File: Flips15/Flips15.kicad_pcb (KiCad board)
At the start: 2 copper layers, 100 x 100 mm, 62 parts, among them U1001 74HC238, U1002 ULN2803A, U1003 74HC238, U1004 TBD62783A, U1101 74HC238, U1102 ULN2803A, U1103 74HC238, U1104 TBD62783A, U201 74LS138, U301 74HC238, U302 ULN2803A, U303 74HC238, U304 TBD62783A, U401 74HC238, U402 ULN2803A, U403 74HC238, U404 TBD62783A, U501 74HC238, U502 ULN2803A, U503 74HC238, U504 TBD62783A, U601 74HC238, U602 ULN2803A, U603 74HC238, U604 TBD62783A, U701 74LS138, U801 74HC238, U802 ULN2803A, U803 74HC238, U804 TBD62783A, U901 74HC238, U902 ULN2803A, U903 74HC238, U904 TBD62783A

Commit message: rework Flips15 draft
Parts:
- U1001, U1003, U1101, U1103, U301, U303, U401, U403, U501, U503, U601, U603, U801, U803, U901, U903: footprint SMD_Packages:SO-16-N -> Housings_SOIC:SOIC-16_3.9x9.9mm_Pitch1.27mm
- U201, U701: value 74LS138 -> 74HC238; footprint SMD_Packages:SO-16-N -> Housings_SOIC:SOIC-16_3.9x9.9mm_Pitch1.27mm
- moved C701 331.5 mm to (88.9, 141.6), turned to 90 degrees
- moved C902 283.5 mm to (64.8, 131.4), turned to 180 degrees
- moved C901 281.3 mm to (101.0, 131.4), turned to 180 degrees
- moved C1101 247.8 mm to (137.8, 131.4), turned to 180 degrees
- moved C302 247.5 mm to (255.4, 120.0)
- moved C301 247.5 mm to (266.7, 105.0)
- moved C1102 234.9 mm to (127.0, 131.4), turned to 180 degrees
- moved C802 232.8 mm to (53.3, 131.4), turned to 180 degrees
- moved C1002 226.9 mm to (76.2, 131.4), turned to 180 degrees
- moved C1001 225.5 mm to (113.0, 131.4), turned to 180 degrees
- moved C801 210.4 mm to (89.5, 131.4), turned to 180 degrees
- moved U201 66.2 mm to (195.6, 132.1), turned to 90 degrees
- moved CNX101 63.5 mm to (198.1, 146.1)
- moved BROSE103 47.3 mm to (117.5, 99.1)
- moved U1004 29.3 mm to (85.1, 108.6)
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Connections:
- net Net-(U1001-Pad10) renamed /UnitY/Group2/YL5
- net Net-(U1001-Pad11) renamed /UnitY/Group2/YL4
- net Net-(U1001-Pad12) renamed /UnitY/Group2/YL3
- net Net-(U1001-Pad13) renamed /UnitY/Group2/YL2
- net Net-(U1001-Pad14) renamed /UnitY/Group2/YL1
- net Net-(U1001-Pad15) renamed /UnitY/Group2/YL0
- net Net-(U1001-Pad7) renamed /UnitY/Group2/YL7
- net Net-(U1001-Pad9) renamed /UnitY/Group2/YL6
- net Net-(U1003-Pad10) renamed /UnitY/Group2/YH5
- net Net-(U1003-Pad11) renamed /UnitY/Group2/YH4
- net Net-(U1003-Pad12) renamed /UnitY/Group2/YH3
- net Net-(U1003-Pad13) renamed /UnitY/Group2/YH2
- net Net-(U1003-Pad14) renamed /UnitY/Group2/YH1
- net Net-(U1003-Pad15) renamed /UnitY/Group2/YH0
- net Net-(U1003-Pad7) renamed /UnitY/Group2/YH7
- net Net-(U1003-Pad9) renamed /UnitY/Group2/YH6
- net Net-(U1101-Pad10) renamed /UnitY/Group3/YL5
- net Net-(U1101-Pad11) renamed /UnitY/Group3/YL4
- net Net-(U1101-Pad12) renamed /UnitY/Group3/YL3
- net Net-(U1101-Pad13) renamed /UnitY/Group3/YL2
- net Net-(U1101-Pad14) renamed /UnitY/Group3/YL1
- net Net-(U1101-Pad15) renamed /UnitY/Group3/YL0
- net Net-(U1101-Pad7) renamed /UnitY/Group3/YL7
- net Net-(U1101-Pad9) renamed /UnitY/Group3/YL6
- net Net-(U1103-Pad10) renamed /UnitY/Group3/YH5
- net Net-(U1103-Pad11) renamed /UnitY/Group3/YH4
- net Net-(U1103-Pad12) renamed /UnitY/Group3/YH3
- net Net-(U1103-Pad13) renamed /UnitY/Group3/YH2
- net Net-(U1103-Pad14) renamed /UnitY/Group3/YH1
- net Net-(U1103-Pad15) renamed /UnitY/Group3/YH0
- net Net-(U1103-Pad7) renamed /UnitY/Group3/YH7
- net Net-(U1103-Pad9) renamed /UnitY/Group3/YH6
- net Net-(U301-Pad10) renamed /UnitX/Group0/YL5
- net Net-(U301-Pad11) renamed /UnitX/Group0/YL4
- net Net-(U301-Pad12) renamed /UnitX/Group0/YL3
- net Net-(U301-Pad13) renamed /UnitX/Group0/YL2
- net Net-(U301-Pad14) renamed /UnitX/Group0/YL1
- net Net-(U301-Pad15) renamed /UnitX/Group0/YL0
- net Net-(U301-Pad7) renamed /UnitX/Group0/YL7
- net Net-(U301-Pad9) renamed /UnitX/Group0/YL6
- net Net-(U303-Pad10) renamed /UnitX/Group0/YH5
- net Net-(U303-Pad11) renamed /UnitX/Group0/YH4
- net Net-(U303-Pad12) renamed /UnitX/Group0/YH3
- net Net-(U303-Pad13) renamed /UnitX/Group0/YH2
- net Net-(U303-Pad14) renamed /UnitX/Group0/YH1
- net Net-(U303-Pad15) renamed /UnitX/Group0/YH0
- net Net-(U303-Pad7) renamed /UnitX/Group0/YH7
- net Net-(U303-Pad9) renamed /UnitX/Group0/YH6
- net Net-(U401-Pad10) renamed /UnitX/Group1/YL5
- net Net-(U401-Pad11) renamed /UnitX/Group1/YL4
- net Net-(U401-Pad12) renamed /UnitX/Group1/YL3
- net Net-(U401-Pad13) renamed /UnitX/Group1/YL2
- net Net-(U401-Pad14) renamed /UnitX/Group1/YL1
- net Net-(U401-Pad15) renamed /UnitX/Group1/YL0
- net Net-(U401-Pad7) renamed /UnitX/Group1/YL7
- net Net-(U401-Pad9) renamed /UnitX/Group1/YL6
- net Net-(U403-Pad10) renamed /UnitX/Group1/YH5
- net Net-(U403-Pad11) renamed /UnitX/Group1/YH4
- net Net-(U403-Pad12) renamed /UnitX/Group1/YH3
- net Net-(U403-Pad13) renamed /UnitX/Group1/YH2
- net Net-(U403-Pad14) renamed /UnitX/Group1/YH1
- net Net-(U403-Pad15) renamed /UnitX/Group1/YH0
- net Net-(U403-Pad7) renamed /UnitX/Group1/YH7
- net Net-(U403-Pad9) renamed /UnitX/Group1/YH6
- net Net-(U501-Pad10) renamed /UnitX/Group2/YL5
- net Net-(U501-Pad11) renamed /UnitX/Group2/YL4
- net Net-(U501-Pad12) renamed /UnitX/Group2/YL3
- net Net-(U501-Pad13) renamed /UnitX/Group2/YL2
- net Net-(U501-Pad14) renamed /UnitX/Group2/YL1
- net Net-(U501-Pad15) renamed /UnitX/Group2/YL0
- net Net-(U501-Pad7) renamed /UnitX/Group2/YL7
- net Net-(U501-Pad9) renamed /UnitX/Group2/YL6
- net Net-(U503-Pad10) renamed /UnitX/Group2/YH5
- net Net-(U503-Pad11) renamed /UnitX/Group2/YH4
- net Net-(U503-Pad12) renamed /UnitX/Group2/YH3
- net Net-(U503-Pad13) renamed /UnitX/Group2/YH2
- net Net-(U503-Pad14) renamed /UnitX/Group2/YH1
- net Net-(U503-Pad15) renamed /UnitX/Group2/YH0
- net Net-(U503-Pad7) renamed /UnitX/Group2/YH7
- net Net-(U503-Pad9) renamed /UnitX/Group2/YH6
- net Net-(U601-Pad10) renamed /UnitX/Group3/YL5
- net Net-(U601-Pad11) renamed /UnitX/Group3/YL4
- net Net-(U601-Pad12) renamed /UnitX/Group3/YL3
- net Net-(U601-Pad13) renamed /UnitX/Group3/YL2
- net Net-(U601-Pad14) renamed /UnitX/Group3/YL1
- net Net-(U601-Pad15) renamed /UnitX/Group3/YL0
- net Net-(U601-Pad7) renamed /UnitX/Group3/YL7
- net Net-(U601-Pad9) renamed /UnitX/Group3/YL6
- net Net-(U603-Pad10) renamed /UnitX/Group3/YH5
- net Net-(U603-Pad11) renamed /UnitX/Group3/YH4
- net Net-(U603-Pad12) renamed /UnitX/Group3/YH3
- net Net-(U603-Pad13) renamed /UnitX/Group3/YH2
- net Net-(U603-Pad14) renamed /UnitX/Group3/YH1
- net Net-(U603-Pad15) renamed /UnitX/Group3/YH0
- net Net-(U603-Pad7) renamed /UnitX/Group3/YH7
- net Net-(U603-Pad9) renamed /UnitX/Group3/YH6
- net Net-(U801-Pad10) renamed /UnitY/Group0/YL5
- net Net-(U801-Pad11) renamed /UnitY/Group0/YL4
- net Net-(U801-Pad12) renamed /UnitY/Group0/YL3
- net Net-(U801-Pad13) renamed /UnitY/Group0/YL2
- net Net-(U801-Pad14) renamed /UnitY/Group0/YL1
- net Net-(U801-Pad15) renamed /UnitY/Group0/YL0
- net Net-(U801-Pad7) renamed /UnitY/Group0/YL7
- net Net-(U801-Pad9) renamed /UnitY/Group0/YL6
- net Net-(U803-Pad10) renamed /UnitY/Group0/YH5
- net Net-(U803-Pad11) renamed /UnitY/Group0/YH4
- net Net-(U803-Pad12) renamed /UnitY/Group0/YH3
- net Net-(U803-Pad13) renamed /UnitY/Group0/YH2
- net Net-(U803-Pad14) renamed /UnitY/Group0/YH1
- net Net-(U803-Pad15) renamed /UnitY/Group0/YH0
- net Net-(U803-Pad7) renamed /UnitY/Group0/YH7
- net Net-(U803-Pad9) renamed /UnitY/Group0/YH6
- net Net-(U901-Pad10) renamed /UnitY/Group1/YL5
- net Net-(U901-Pad11) renamed /UnitY/Group1/YL4
- net Net-(U901-Pad12) renamed /UnitY/Group1/YL3
- net Net-(U901-Pad13) renamed /UnitY/Group1/YL2
- net Net-(U901-Pad14) renamed /UnitY/Group1/YL1
- net Net-(U901-Pad15) renamed /UnitY/Group1/YL0
- net Net-(U901-Pad7) renamed /UnitY/Group1/YL7
- net Net-(U901-Pad9) renamed /UnitY/Group1/YL6
- net Net-(U903-Pad10) renamed /UnitY/Group1/YH5
- net Net-(U903-Pad11) renamed /UnitY/Group1/YH4
- net Net-(U903-Pad12) renamed /UnitY/Group1/YH3
- net Net-(U903-Pad13) renamed /UnitY/Group1/YH2
- net Net-(U903-Pad14) renamed /UnitY/Group1/YH1
- net Net-(U903-Pad15) renamed /UnitY/Group1/YH0
- net Net-(U903-Pad7) renamed /UnitY/Group1/YH7
- net Net-(U903-Pad9) renamed /UnitY/Group1/YH6
- U1001 pad 4: /UnitY/Group2/~GE -> GND
- U1001 pad 5: /UnitY/DATA -> GND
- U1001 pad 6: VCC -> /UnitY/E2L
- U1003 pad 4: /UnitY/Group2/~GE -> GND
- U1003 pad 6: /UnitY/DATA -> /UnitY/E2H
- U1101 pad 4: /UnitY/Group3/~GE -> GND
- U1101 pad 5: /UnitY/DATA -> GND
- U1101 pad 6: VCC -> /UnitY/E3L
- U1103 pad 4: /UnitY/Group3/~GE -> GND
- U1103 pad 6: /UnitY/DATA -> /UnitY/E3H
- U201 pad 1: /UnitX/B0 -> /UnitX/DATA
- U201 pad 10: Net-(U201-Pad10) -> /UnitX/E2H
- U201 pad 11: Net-(U201-Pad11) -> /UnitX/E2L
- U201 pad 12: /UnitX/Group3/~GE -> /UnitX/E1H
- U201 pad 13: /UnitX/Group2/~GE -> /UnitX/E1L
- U201 pad 14: /UnitX/Group1/~GE -> /UnitX/E0H
- U201 pad 15: /UnitX/Group0/~GE -> /UnitX/E0L
- U201 pad 2: /UnitX/B1 -> /UnitX/B0
- U201 pad 3: GND -> /UnitX/B1
- U201 pad 7: Net-(U201-Pad7) -> /UnitX/E3H
- U201 pad 9: Net-(U201-Pad9) -> /UnitX/E3L
- U301 pad 4: /UnitX/Group0/~GE -> GND
- U301 pad 5: /UnitX/DATA -> GND
- U301 pad 6: VCC -> /UnitX/E0L
- U303 pad 4: /UnitX/Group0/~GE -> GND
- U303 pad 6: /UnitX/DATA -> /UnitX/E0H
- U401 pad 4: /UnitX/Group1/~GE -> GND
- U401 pad 5: /UnitX/DATA -> GND
- U401 pad 6: VCC -> /UnitX/E1L
- U403 pad 4: /UnitX/Group1/~GE -> GND
- U403 pad 6: /UnitX/DATA -> /UnitX/E1H
- U501 pad 4: /UnitX/Group2/~GE -> GND
- U501 pad 5: /UnitX/DATA -> GND
- U501 pad 6: VCC -> /UnitX/E2L
- U503 pad 4: /UnitX/Group2/~GE -> GND
- U503 pad 6: /UnitX/DATA -> /UnitX/E2H
- U601 pad 4: /UnitX/Group3/~GE -> GND
- U601 pad 5: /UnitX/DATA -> GND
- U601 pad 6: VCC -> /UnitX/E3L
- U603 pad 4: /UnitX/Group3/~GE -> GND
- U603 pad 6: /UnitX/DATA -> /UnitX/E3H
- U701 pad 1: /UnitY/B0 -> /UnitY/DATA
- U701 pad 10: Net-(U701-Pad10) -> /UnitY/E2H
- U701 pad 11: Net-(U701-Pad11) -> /UnitY/E2L
- U701 pad 12: /UnitY/Group3/~GE -> /UnitY/E1H
- U701 pad 13: /UnitY/Group2/~GE -> /UnitY/E1L
- U701 pad 14: /UnitY/Group1/~GE -> /UnitY/E0H
- U701 pad 15: /UnitY/Group0/~GE -> /UnitY/E0L
- U701 pad 2: /UnitY/B1 -> /UnitY/B0
- U701 pad 3: GND -> /UnitY/B1
- U701 pad 7: Net-(U701-Pad7) -> /UnitY/E3H
- U701 pad 9: Net-(U701-Pad9) -> /UnitY/E3L
- U801 pad 4: /UnitY/Group0/~GE -> GND
- U801 pad 5: /UnitY/DATA -> GND
- U801 pad 6: VCC -> /UnitY/E0L
- U803 pad 4: /UnitY/Group0/~GE -> GND
- U803 pad 6: /UnitY/DATA -> /UnitY/E0H
- U901 pad 4: /UnitY/Group1/~GE -> GND
- U901 pad 5: /UnitY/DATA -> GND
- U901 pad 6: VCC -> /UnitY/E1L
- U903 pad 4: /UnitY/Group1/~GE -> GND
- U903 pad 6: /UnitY/DATA -> /UnitY/E1H
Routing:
- net /UnitX/Group2/YH0: track 28.6 -> 0.00 mm
- net /UnitX/Group2/YL0: track 26.7 -> 0.00 mm
- net /UnitX/Group2/YH1: track 23.3 -> 0.00 mm
- net /UnitX/Group2/YL1: track 22.8 -> 0.00 mm
- net /UnitX/Group2/YH2: track 20.3 -> 0.00 mm
- net /UnitX/Group2/YL2: track 19.7 -> 0.00 mm
- net /UnitX/Group2/YH3: track 17.2 -> 0.00 mm
- net /UnitX/Group2/YL3: track 17.1 -> 0.00 mm
- net /UnitX/Group2/YL4: track 14.7 -> 0.00 mm
- net /UnitX/Group2/YL7: track 14.7 -> 0.00 mm
- net /UnitX/Group2/YH4: track 14.7 -> 0.00 mm
- net /UnitX/Group2/YH5: track 14.0 -> 0.00 mm
- net /UnitX/Group2/YH7: track 13.3 -> 0.00 mm
- net /UnitX/Group2/YL5: track 12.4 -> 0.00 mm
- net /X21: track 12.0 -> 0.00 mm
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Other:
- net class DrivingCurrent added: clearance 0.2, trace_width 0.5, via_dia 0.8, via_drill 0.4

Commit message: Flips15 to only use 1 unit
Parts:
- removed BRDIC101, BROSE102: Conn_02x17_Odd_Even, Own:Pin_Header_Angle_Shrouded_2x17_Pitch2.54mm_ConvNumbering
- removed BROSE101: Conn_02x30_Odd_Even, Own:Pin_Header_Straight_Shrouded_2x30_Pitch2.54mm_ConvNumbering
- removed BROSE103: Conn_02x10_Odd_Even, Own:Pin_Header_Straight_Shrouded_2x10_Pitch2.54mm_ConvNumbering
- removed C201, C301, C302, C401, C402, C501, C502, C601, C602: 0μ1, Capacitors_SMD:C_0805_HandSoldering
- removed CNX101, CNY101: UFP2810, Own:Pin_Header_Angle_Shrouded_2x05_Pitch2.54mm_ConvNumbering
- removed REF** (x4): MountingHole_3.2mm_M3, Mounting_Holes:MountingHole_3.2mm_M3
- removed U201, U301, U303, U401, U403, U501, U503, U601, U603: 74HC238, Housings_SOIC:SOIC-16_3.9x9.9mm_Pitch1.27mm
- removed U302, U402, U502, U602: ULN2803A, Housings_DIP:DIP-18_W7.62mm_Socket
- removed U304, U404, U504, U604: TBD62783A, Housings_DIP:DIP-18_W7.62mm_Socket
- added BRDIC1: Conn_02x17_Odd_Even, Own:Pin_Header_Straight_Shrouded_Locks_2x17_Pitch2.54mm_ConvNumbering, F.Cu at (138.4, 64.8)
- added BROSE20: Conn_02x10_Odd_Even, Own:Pin_Header_Straight_Shrouded_Locks_2x10_Pitch2.54mm_ConvNumbering, F.Cu at (115.6, 100.3)
- added BROSE34: Conn_02x17_Odd_Even, Own:Pin_Header_Straight_Shrouded_Locks_2x17_Pitch2.54mm_ConvNumbering, F.Cu at (80.0, 57.1)
- added BROSE60: Conn_02x30_Odd_Even, Own:Pin_Header_Straight_Shrouded_Locks_2x30_Pitch2.54mm_ConvNumbering, F.Cu at (64.8, 90.2)
- added CN1: UFP2810, Own:Pin_Header_Angle_Shrouded_2x05_Pitch2.54mm_ConvNumbering, F.Cu at (102.1, 17.5)
- added JP101: Jumper_NO_Small, Own:SolderJumper1.3mm, B.Cu at (131.1, 10.7)
- added JP102: Jumper_NO_Small, Own:SolderJumper1.3mm, F.Cu at (131.4, 23.5)
- added JP103: Jumper_NO_Small, Own:SolderJumper1.3mm, F.Cu at (137.3, 10.5)
- added JP104: Jumper_NO_Small, Own:SolderJumper1.3mm, F.Cu at (131.4, 34.5)
- added JP105: Jumper_NO_Small, Own:SolderJumper1.3mm, F.Cu at (137.8, 23.5)
- added JP106: Jumper_NO_Small, Own:SolderJumper1.3mm, F.Cu at (144.7, 10.5)
- added JP107: Jumper_NO_Small, Own:SolderJumper1.3mm, F.Cu at (131.4, 41.9)
- added JP108: Jumper_NO_Small, Own:SolderJumper1.3mm, F.Cu at (137.8, 34.5)
- added JP109: Jumper_NO_Small, Own:SolderJumper1.3mm, F.Cu at (145.2, 23.5)
- added JP110: Jumper_NO_Small, Own:SolderJumper1.3mm, F.Cu at (149.5, 10.5)
- added JP111: Jumper_NO_Small, Own:SolderJumper1.3mm, F.Cu at (137.8, 41.9)
- added JP112: Jumper_NO_Small, Own:SolderJumper1.3mm, F.Cu at (145.2, 34.5)
- added JP113: Jumper_NO_Small, Own:SolderJumper1.3mm, F.Cu at (150.0, 23.5)
- added JP114: Jumper_NO_Small, Own:SolderJumper1.3mm, F.Cu at (155.9, 10.5)
- added JP115: Jumper_NO_Small, Own:SolderJumper1.3mm, F.Cu at (145.2, 41.9)
- added JP116: Jumper_NO_Small, Own:SolderJumper1.3mm, F.Cu at (150.0, 34.5)
- added JP117: Jumper_NO_Small, Own:SolderJumper1.3mm, F.Cu at (156.4, 23.5)
- added JP118: Jumper_NO_Small, Own:SolderJumper1.3mm, F.Cu at (164.0, 10.5)
- added JP119: Jumper_NO_Small, Own:SolderJumper1.3mm, F.Cu at (150.0, 41.9)
- added JP120: Jumper_NO_Small, Own:SolderJumper1.3mm, F.Cu at (156.4, 34.5)
- added JP121: Jumper_NO_Small, Own:SolderJumper1.3mm, F.Cu at (164.6, 23.5)
- added JP122: Jumper_NO_Small, Own:SolderJumper1.3mm, B.Cu at (115.6, 73.7)
- added JP123: Jumper_NO_Small, Own:SolderJumper1.3mm, F.Cu at (156.4, 41.9)
- added JP124: Jumper_NO_Small, Own:SolderJumper1.3mm, F.Cu at (164.6, 34.5)
- added JP125: Jumper_NO_Small, Own:SolderJumper1.3mm, F.Cu at (172.7, 23.5)
- added JP126: Jumper_NO_Small, Own:SolderJumper1.3mm, F.Cu at (164.6, 41.9)
- added JP127: Jumper_NO_Small, Own:SolderJumper1.3mm, F.Cu at (172.7, 34.5)
- added JP128: Jumper_NO_Small, Own:SolderJumper1.3mm, F.Cu at (172.7, 41.9)
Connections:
- U1002 pad 11: /~RY21 -> /X21
- U1002 pad 12: /~RY20 -> /X20
- U1002 pad 13: /~RY19 -> /X19
- U1002 pad 14: /~RY18 -> /X18
- U1002 pad 15: /~RY17 -> /X17
- U1002 pad 16: /~RY16 -> /X16
- U1002 pad 17: /~RY15 -> /X15
- U1102 pad 11: /~RY28 -> /X28
- U1102 pad 12: /~RY27 -> /X27
- U1102 pad 13: /~RY26 -> /X26
- U1102 pad 14: /~RY25 -> /X25
- U1102 pad 15: /~RY24 -> /X24
- U1102 pad 16: /~RY23 -> /X23
- U1102 pad 17: /~RY22 -> /X22
- U802 pad 11: /~RY7 -> /X7
- U802 pad 12: /~RY6 -> /X6
- U802 pad 13: /~RY5 -> /X5
- U802 pad 14: /~RY4 -> /X4
- U802 pad 15: /~RY3 -> /X3
- U802 pad 16: /~RY2 -> /X2
- U802 pad 17: /~RY1 -> /X1
- U902 pad 11: /~RY14 -> /X14
- U902 pad 12: /~RY13 -> /X13
- U902 pad 13: /~RY12 -> /X12
- U902 pad 14: /~RY11 -> /X11
- U902 pad 15: /~RY10 -> /X10
- U902 pad 16: /~RY9 -> /X9
- U902 pad 17: /~RY8 -> /X8

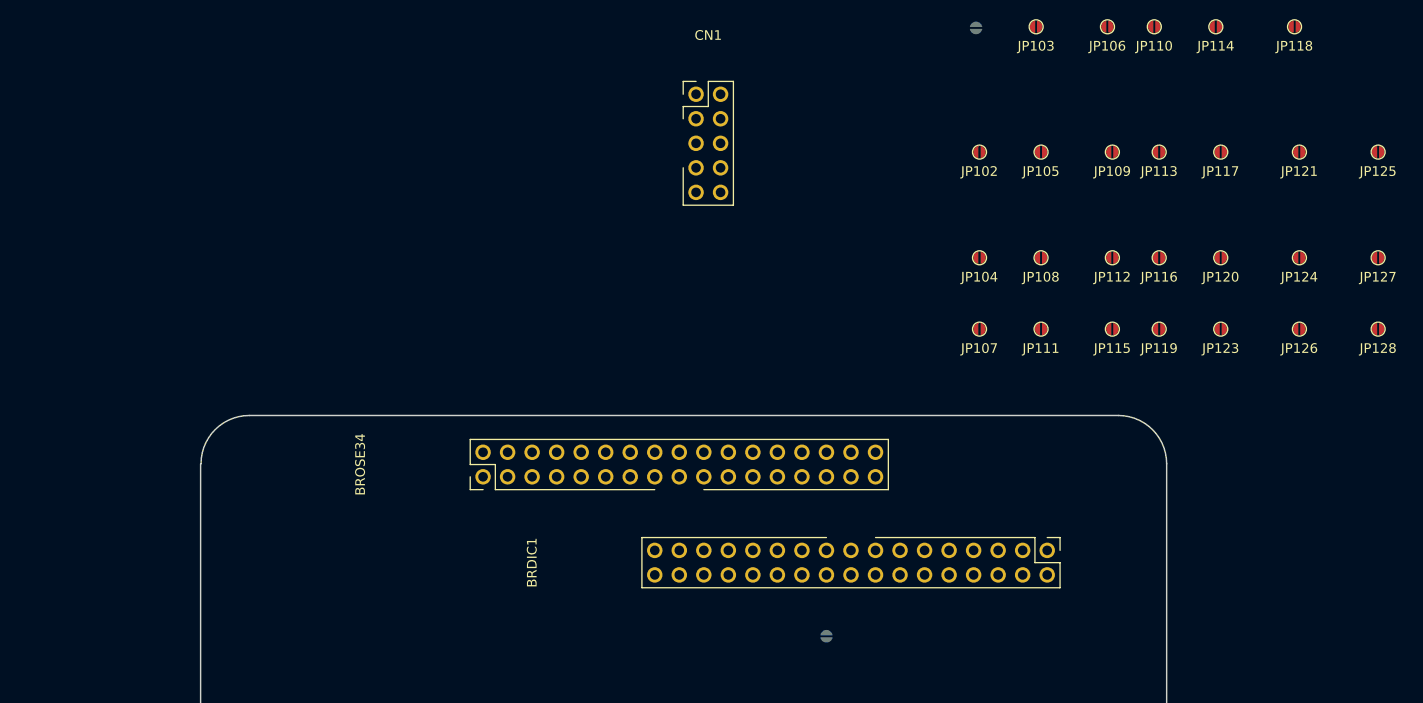
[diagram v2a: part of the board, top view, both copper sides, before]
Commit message: experimenting with solder jumpers at BRDIC1 connector
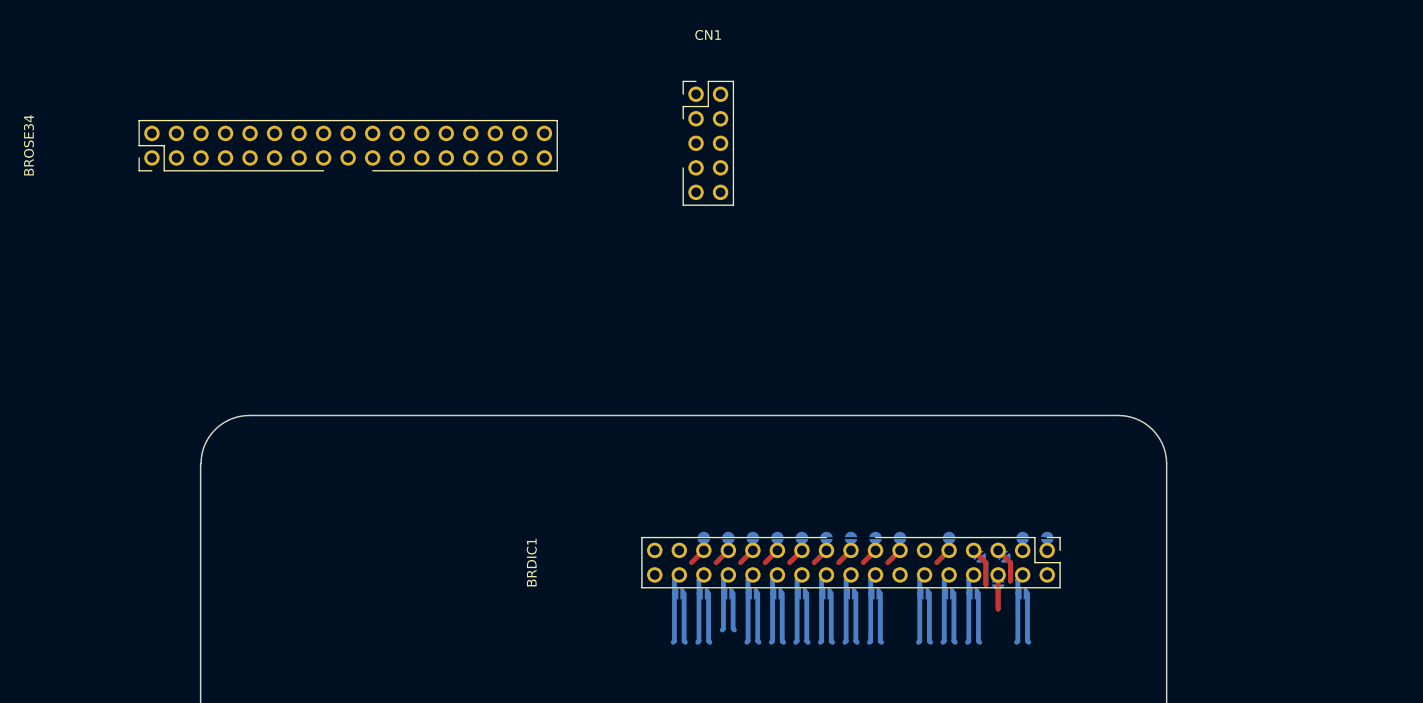
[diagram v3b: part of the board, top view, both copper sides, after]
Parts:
- JP101, JP122: footprint Own:SolderJumper1.3mm -> Own:SolderJumper1.3mmNoSilk
- JP102, JP103, JP104, JP105, JP106, JP107, JP108, JP109, JP110, JP111, JP112, JP113, JP114, JP115, JP116, JP117, JP118, JP119, JP120, JP121, JP123, JP124, JP125, JP126, JP127, JP128: footprint Own:SolderJumper1.3mm -> Own:SolderJumper1.3mmNoSilk; moved to B.Cu
- moved JP125 73.9 mm to (110.5, 63.5), turned to 270 degrees
- moved JP114 69.8 mm to (118.1, 69.2), turned to 180 degrees
- moved JP106 67.9 mm to (110.5, 69.2), turned to 180 degrees
- moved JP103 66.8 mm to (105.4, 69.2), turned to 180 degrees
- moved JP127 66.4 mm to (113.0, 63.5), turned to 270 degrees
- moved JP101 66.1 mm to (100.3, 69.2), turned to 180 degrees
- moved JP124 63.6 mm to (108.0, 63.5), turned to 270 degrees
- moved JP110 61.6 mm to (130.8, 69.2), turned to 180 degrees
- moved JP121 59.4 mm to (120.7, 63.5), turned to 270 degrees
- moved JP118 58.8 mm to (138.4, 63.5), turned to 270 degrees
- moved JP128 58.7 mm to (118.1, 63.5), turned to 270 degrees
- moved JP123 55.4 mm to (105.4, 63.5), turned to 270 degrees
- moved JP102 53.9 mm to (102.9, 69.2), turned to 180 degrees
- moved JP126 53.5 mm to (115.6, 63.5), turned to 270 degrees
- moved JP105 52.0 mm to (113.0, 69.2), turned to 180 degrees
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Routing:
- net /X9: track 0.00 -> 7.25 mm
- net /X8: track 0.00 -> 7.25 mm
- net /X5: track 0.00 -> 7.25 mm
- net /X4: track 0.00 -> 7.25 mm
- net /X2: track 0.00 -> 7.25 mm
- net /X14: track 0.00 -> 7.25 mm
- net /X12: track 0.00 -> 7.25 mm
- net /X1: track 0.00 -> 7.25 mm
- net /X7: track 0.00 -> 7.25 mm
- net /X6: track 0.00 -> 7.25 mm
- net /X11: track 0.00 -> 7.25 mm
- net /X10: track 0.00 -> 7.25 mm
- net /X16: track 0.00 -> 6.77 mm
- net /X3: track 0.00 -> 5.98 mm
- net /SY11: track 0.00 -> 5.14 mm
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
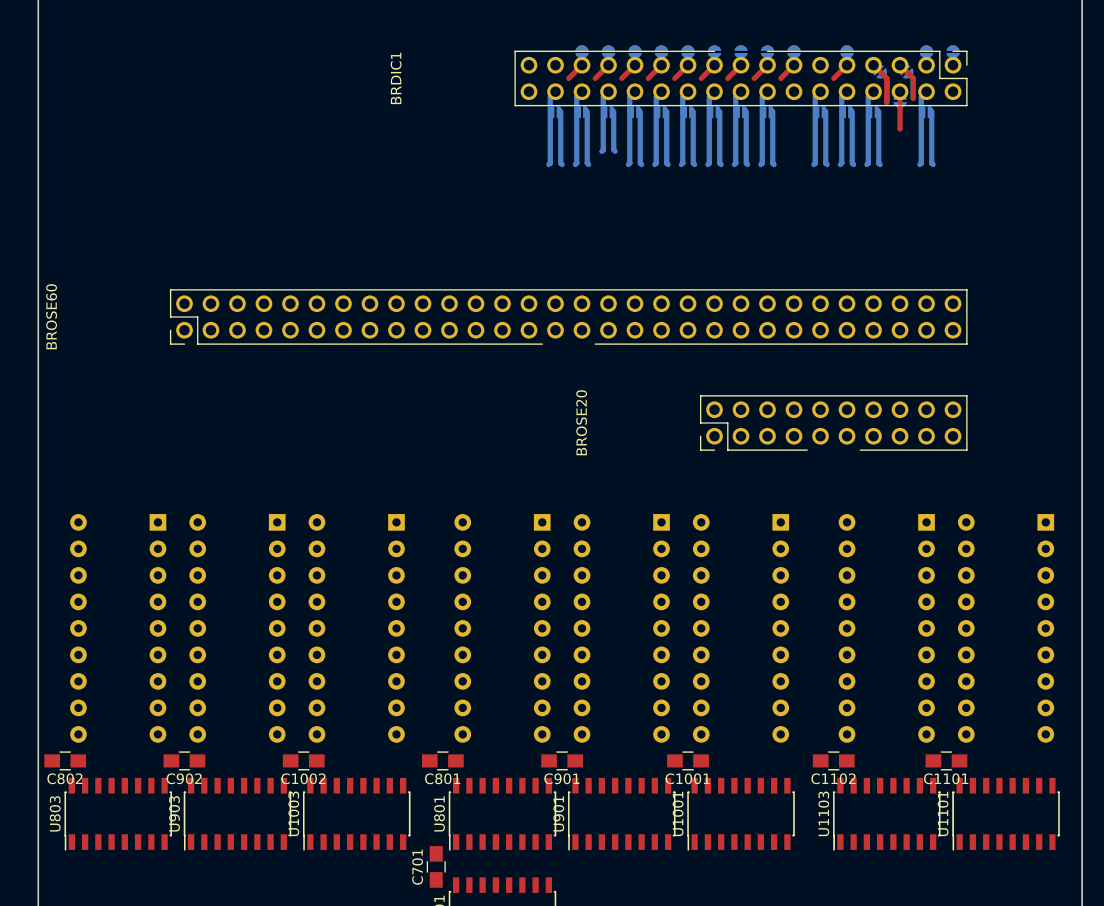
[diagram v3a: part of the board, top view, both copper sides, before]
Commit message: adding traces for flips 15
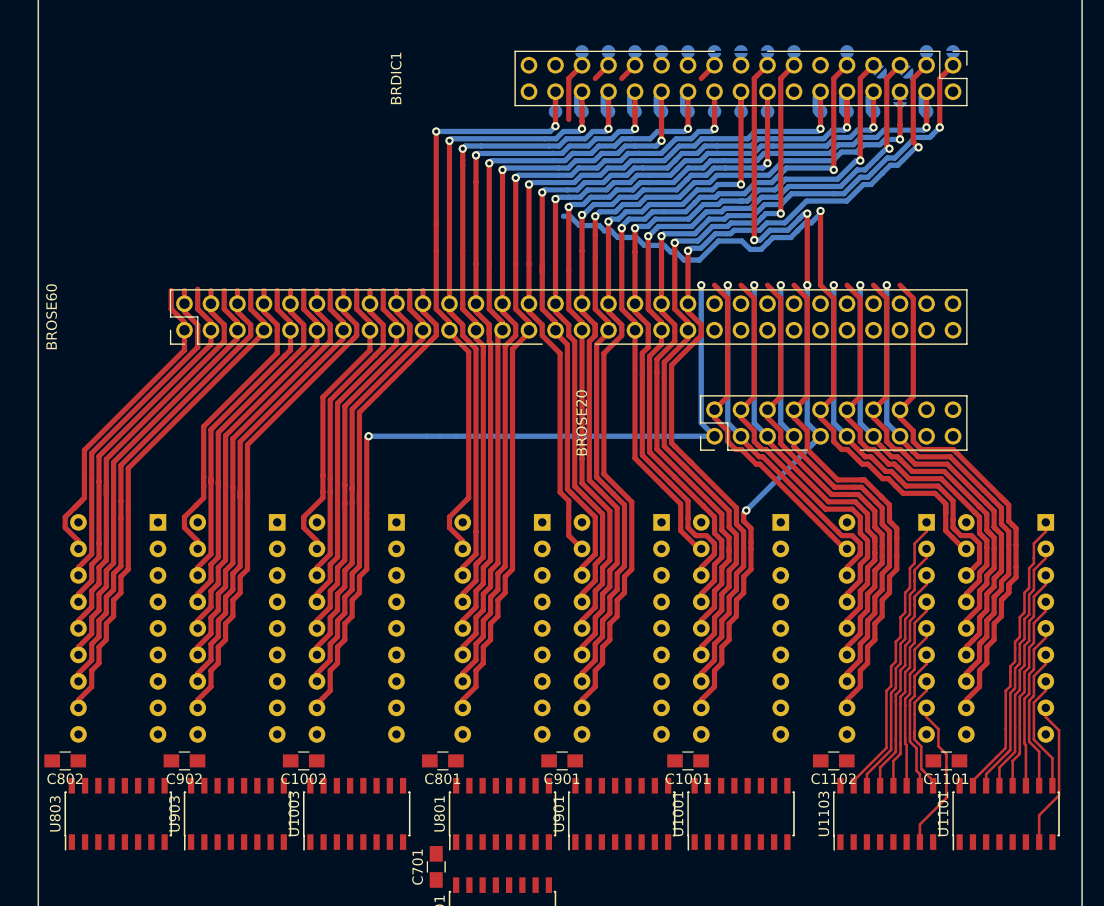
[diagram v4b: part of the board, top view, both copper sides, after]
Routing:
- net /X20: track 0.77 -> 83.4 mm, vias 0 -> 2
- net /X11: track 7.25 -> 89.3 mm, vias 0 -> 2
- net /X13: track 3.56 -> 85.2 mm, vias 0 -> 2
- net /X18: track 0.77 -> 81.0 mm, vias 0 -> 2
- net /X21: track 2.57 -> 79.7 mm, vias 0 -> 4
- net /SY21: track 0.00 -> 76.2 mm, vias 0 -> 2
- net /X22: track 2.57 -> 78.7 mm, vias 0 -> 1
- net /X9: track 7.25 -> 80.6 mm, vias 0 -> 2
- net /X10: track 7.25 -> 80.2 mm, vias 0 -> 2
- net /X7: track 7.25 -> 79.8 mm, vias 0 -> 2
- net /X17: track 3.70 -> 74.9 mm, vias 0 -> 2
- net /X19: track 2.57 -> 72.7 mm, vias 0 -> 2
- net /X5: track 7.25 -> 75.3 mm, vias 0 -> 2
- net /X14: track 7.25 -> 75.3 mm, vias 0 -> 2
- net /X6: track 7.25 -> 74.9 mm, vias 0 -> 2
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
